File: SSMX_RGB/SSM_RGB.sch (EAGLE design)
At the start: 24 parts, among them IC1 CBT3244ADW, IC2 CBT3244ADW, IC3 CBT3244ADW, IC4 CBT3244ADW, U1 L7805C-V

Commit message: Revision
*Tied S_PWR Pos 1 to nothing (no power on this pos)
*Addressed errors and warnings in ERC
*Ran Autorouter again to fix netlist
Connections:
- net BUS_V-: no longer S_PWR.O
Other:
- moved on the sheet: R2
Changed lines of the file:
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@@
 <instance part="IC4" gate="G$1" x="8.89" y="-19.558" rot="R90"/>
 <instance part="R1" gate="G$1" x="55.88" y="101.6" rot="R90"/>
-<instance part="R2" gate="G$1" x="-12.7" y="-10.16" rot="R90"/>
+<instance part="R2" gate="G$1" x="-10.16" y="-10.16" rot="R90"/>
 <instance part="R3" gate="G$1" x="-78.74" y="76.2" rot="R270"/>
 <instance part="R4" gate="G$1" x="-27.432" y="84.328" rot="R180"/>
@@
 <net name="BUS_V-" class="0">
 <segment>
-<pinref part="S_PWR" gate="1" pin="O"/>
-<wire x1="-40.64" y1="106.68" x2="-38.1" y2="106.68" width="0.1524" layer="91"/>
-<wire x1="-38.1" y1="106.68" x2="-38.1" y2="99.06" width="0.1524" layer="91"/>
 <wire x1="-38.1" y1="99.06" x2="-55.88" y2="99.06" width="0.1524" layer="91"/>
 <wire x1="-17.78" y1="96.52" x2="-38.1" y2="96.52" width="0.1524" layer="91"/>
 <wire x1="-38.1" y1="96.52" x2="-38.1" y2="99.06" width="0.1524" layer="91"/>
-<junction x="-38.1" y="99.06"/>
 <pinref part="IC3" gate="G$1" pin="GND"/>
 <wire x1="17.78" y1="86.868" x2="15.24" y2="86.868" width="0.1524" layer="91"/>
@@
 <pinref part="IC3" gate="G$1" pin="VCC"/>
 <wire x1="17.78" y1="91.948" x2="-2.54" y2="91.948" width="0.1524" layer="91"/>
-<pinref part="IC1" gate="G$1" pin="VCC"/>
-<wire x1="-32.512" y1="40.64" x2="-32.512" y2="20.32" width="0.1524" layer="91"/>
-<wire x1="-32.512" y1="20.32" x2="-2.54" y2="20.32" width="0.1524" layer="91"/>
 <wire x1="-2.54" y1="20.32" x2="-2.54" y2="84.328" width="0.1524" layer="91"/>
-<pinref part="IC2" gate="G$1" pin="VCC"/>
 <wire x1="-2.54" y1="84.328" x2="-2.54" y2="91.948" width="0.1524" layer="91"/>
-<wire x1="-78.486" y1="20.32" x2="-78.486" y2="15.24" width="0.1524" layer="91"/>
-<wire x1="-78.486" y1="15.24" x2="-32.512" y2="15.24" width="0.1524" layer="91"/>
-<wire x1="-32.512" y1="15.24" x2="-32.512" y2="20.32" width="0.1524" layer="91"/>
-<junction x="-32.512" y="20.32"/>
-<wire x1="-32.512" y1="15.24" x2="-27.94" y2="15.24" width="0.1524" layer="91"/>
-<pinref part="IC4" gate="G$1" pin="VCC"/>
-<wire x1="25.4" y1="-22.098" x2="30.48" y2="-22.098" width="0.1524" layer="91"/>
-<wire x1="30.48" y1="-22.098" x2="30.48" y2="-2.54" width="0.1524" layer="91"/>
-<wire x1="30.48" y1="-2.54" x2="-12.7" y2="-2.54" width="0.1524" layer="91"/>
-<wire x1="-12.7" y1="-2.54" x2="-27.94" y2="-2.54" width="0.1524" layer="91"/>
-<wire x1="-27.94" y1="15.24" x2="-27.94" y2="-2.54" width="0.1524" layer="91"/>
 <pinref part="R4" gate="G$1" pin="1"/>
 <wire x1="-22.352" y1="84.328" x2="-2.54" y2="84.328" width="0.1524" layer="91"/>
 <junction x="-2.54" y="84.328"/>
-<pinref part="R2" gate="G$1" pin="2"/>
-<wire x1="-12.7" y1="-5.08" x2="-12.7" y2="-2.54" width="0.1524" layer="91"/>
-<junction x="-12.7" y="-2.54"/>
 <pinref part="R1" gate="G$1" pin="2"/>
 <wire x1="55.88" y1="116.84" x2="55.88" y2="106.68" width="0.1524" layer="91"/>
@@
 <junction x="-2.54" y="91.948"/>
 <label x="2.54" y="116.84" size="1.778" layer="95"/>
+<pinref part="IC1" gate="G$1" pin="VCC"/>
+<wire x1="-32.512" y1="40.64" x2="-38.1" y2="40.64" width="0.1524" layer="91"/>
+<wire x1="-38.1" y1="40.64" x2="-38.1" y2="20.32" width="0.1524" layer="91"/>
+<wire x1="-38.1" y1="20.32" x2="-2.54" y2="20.32" width="0.1524" layer="91"/>
+<pinref part="IC2" gate="G$1" pin="VCC"/>
+<wire x1="-78.486" y1="20.32" x2="-78.486" y2="15.24" width="0.1524" layer="91"/>
+<wire x1="-78.486" y1="15.24" x2="-38.1" y2="15.24" width="0.1524" layer="91"/>
+<wire x1="-38.1" y1="15.24" x2="-27.94" y2="15.24" width="0.1524" layer="91"/>
+<wire x1="-27.94" y1="15.24" x2="-27.94" y2="-2.54" width="0.1524" layer="91"/>
+<wire x1="-10.16" y1="-2.54" x2="-27.94" y2="-2.54" width="0.1524" layer="91"/>
+<pinref part="R2" gate="G$1" pin="2"/>
+<wire x1="-10.16" y1="-5.08" x2="-10.16" y2="-2.54" width="0.1524" layer="91"/>
+<junction x="-10.16" y="-2.54"/>
+<wire x1="30.48" y1="-2.54" x2="-10.16" y2="-2.54" width="0.1524" layer="91"/>
+<wire x1="30.48" y1="-22.098" x2="30.48" y2="-2.54" width="0.1524" layer="91"/>
+<pinref part="IC4" gate="G$1" pin="VCC"/>
+<wire x1="25.4" y1="-22.098" x2="30.48" y2="-22.098" width="0.1524" layer="91"/>
+<wire x1="-38.1" y1="20.32" x2="-38.1" y2="15.24" width="0.1524" layer="91"/>
+<junction x="-38.1" y="20.32"/>
+<junction x="-38.1" y="15.24"/>
 </segment>
 </net>
@@
 <pinref part="U1" gate="G$1" pin="IN"/>
 <wire x1="-35.56" y1="101.6" x2="-35.56" y2="106.68" width="0.1524" layer="91"/>
-</segment>
-</net>
-<net name="N$1" class="0">
-<segment>
-<pinref part="S_AV" gate="G$1" pin="3"/>
-<wire x1="12.7" y1="101.6" x2="53.34" y2="101.6" width="0.1524" layer="91"/>
-<wire x1="53.34" y1="101.6" x2="53.34" y2="83.82" width="0.1524" layer="91"/>
-<wire x1="53.34" y1="83.82" x2="55.88" y2="83.82" width="0.1524" layer="91"/>
-<pinref part="IC3" gate="G$1" pin="!EB"/>
-<pinref part="IC3" gate="G$1" pin="!EA"/>
-<wire x1="50.8" y1="91.948" x2="55.88" y2="91.948" width="0.1524" layer="91"/>
-<pinref part="R1" gate="G$1" pin="1"/>
-<wire x1="55.88" y1="96.52" x2="55.88" y2="91.948" width="0.1524" layer="91"/>
-<wire x1="55.88" y1="91.948" x2="55.88" y2="86.868" width="0.1524" layer="91"/>
-<wire x1="55.88" y1="86.868" x2="50.8" y2="86.868" width="0.1524" layer="91"/>
-<wire x1="55.88" y1="83.82" x2="55.88" y2="86.868" width="0.1524" layer="91"/>
-<junction x="55.88" y="86.868"/>
-<wire x1="12.7" y1="101.6" x2="12.7" y2="76.2" width="0.1524" layer="91"/>
-<wire x1="12.7" y1="76.2" x2="-15.24" y2="76.2" width="0.1524" layer="91"/>
-<junction x="12.7" y="101.6"/>
-<wire x1="-15.24" y1="76.2" x2="-15.24" y2="-25.4" width="0.1524" layer="91"/>
-<wire x1="-15.24" y1="-25.4" x2="-12.7" y2="-25.4" width="0.1524" layer="91"/>
-<pinref part="IC4" gate="G$1" pin="!EA"/>
-<wire x1="-12.7" y1="-22.098" x2="-7.62" y2="-22.098" width="0.1524" layer="91"/>
-<wire x1="-12.7" y1="-17.018" x2="-12.7" y2="-22.098" width="0.1524" layer="91"/>
-<pinref part="R2" gate="G$1" pin="1"/>
-<wire x1="-12.7" y1="-15.24" x2="-12.7" y2="-17.018" width="0.1524" layer="91"/>
-<pinref part="IC4" gate="G$1" pin="!EB"/>
-<wire x1="-7.62" y1="-17.018" x2="-12.7" y2="-17.018" width="0.1524" layer="91"/>
-<wire x1="-12.7" y1="-25.4" x2="-12.7" y2="-22.098" width="0.1524" layer="91"/>
-<junction x="-12.7" y="-22.098"/>
 </segment>
 </net>
@@
 </segment>
 </net>
+<net name="N$1" class="0">
+<segment>
+<pinref part="IC3" gate="G$1" pin="!EB"/>
+<pinref part="R1" gate="G$1" pin="1"/>
+<wire x1="55.88" y1="96.52" x2="55.88" y2="91.948" width="0.1524" layer="91"/>
+<pinref part="IC3" gate="G$1" pin="!EA"/>
+<wire x1="50.8" y1="91.948" x2="55.88" y2="91.948" width="0.1524" layer="91"/>
+<junction x="55.88" y="91.948"/>
+<wire x1="55.88" y1="91.948" x2="55.88" y2="86.868" width="0.1524" layer="91"/>
+<wire x1="53.34" y1="106.68" x2="53.34" y2="83.82" width="0.1524" layer="91"/>
+<wire x1="53.34" y1="83.82" x2="55.88" y2="83.82" width="0.1524" layer="91"/>
+<wire x1="55.88" y1="83.82" x2="55.88" y2="86.868" width="0.1524" layer="91"/>
+<junction x="55.88" y="86.868"/>
+<wire x1="55.88" y1="86.868" x2="50.8" y2="86.868" width="0.1524" layer="91"/>
+<wire x1="53.34" y1="106.68" x2="17.78" y2="106.68" width="0.1524" layer="91"/>
+<wire x1="17.78" y1="106.68" x2="17.78" y2="101.6" width="0.1524" layer="91"/>
+<pinref part="S_AV" gate="G$1" pin="3"/>
+<wire x1="12.7" y1="101.6" x2="12.7" y2="76.2" width="0.1524" layer="91"/>
+<wire x1="12.7" y1="76.2" x2="-12.7" y2="76.2" width="0.1524" layer="91"/>
+<wire x1="-12.7" y1="76.2" x2="-12.7" y2="46.99" width="0.1524" layer="91"/>
+<wire x1="-12.7" y1="46.99" x2="-13.97" y2="46.99" width="0.1524" layer="91"/>
+<pinref part="IC4" gate="G$1" pin="!EA"/>
+<wire x1="-10.16" y1="-22.098" x2="-7.62" y2="-22.098" width="0.1524" layer="91"/>
+<junction x="-10.16" y="-22.098"/>
+<wire x1="-10.16" y1="-22.098" x2="-13.97" y2="-22.098" width="0.1524" layer="91"/>
+<pinref part="R2" gate="G$1" pin="1"/>
+<wire x1="-10.16" y1="-15.24" x2="-10.16" y2="-17.018" width="0.1524" layer="91"/>
+<wire x1="-10.16" y1="-17.018" x2="-10.16" y2="-22.098" width="0.1524" layer="91"/>
+<junction x="-10.16" y="-17.018"/>
+<pinref part="IC4" gate="G$1" pin="!EB"/>
+<wire x1="-7.62" y1="-17.018" x2="-10.16" y2="-17.018" width="0.1524" layer="91"/>
+<wire x1="-13.97" y1="46.99" x2="-13.97" y2="-22.098" width="0.1524" layer="91"/>
+<wire x1="17.78" y1="101.6" x2="12.7" y2="101.6" width="0.1524" layer="91"/>
+<junction x="12.7" y="101.6"/>
+</segment>
+</net>
 </nets>
 </sheet>
 </sheets>
+<errors>
+</errors>
 </schematic>
 </drawing>

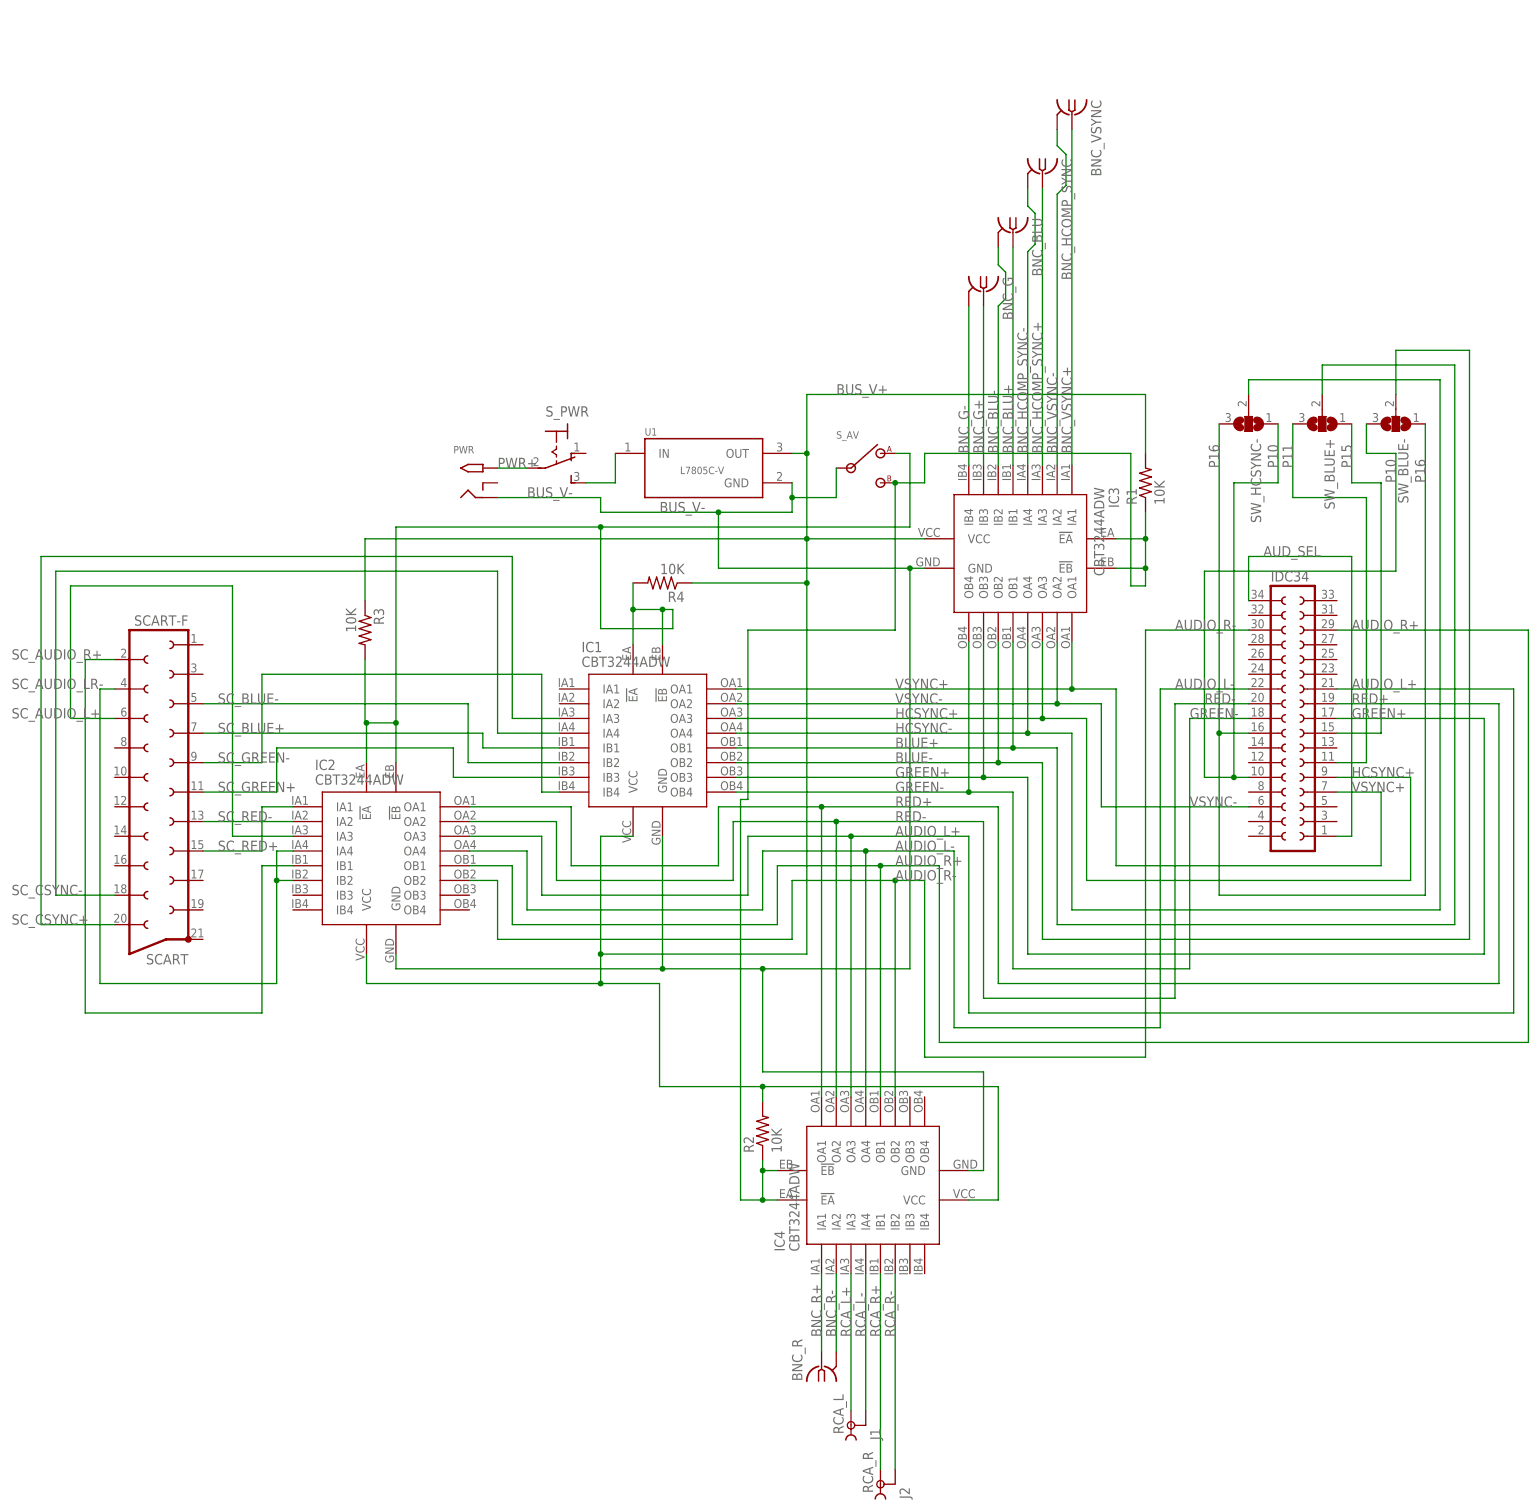
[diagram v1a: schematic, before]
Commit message: Final PCB revisions
SSM & X:
*Renamed BNC_HComp_Sync to just BNC_HCSYNC
*Renamed "Normal" cable type to "Nonstd"
*Removed stray line segs in PCB Art

SSM:
*Added warning about using both AV sources

X:
*Renamed VReg and Bus Sw IC components to Ux series
*Renamed both switchs to Sx series
*Renamed "PWR" to "J1"

Documentation:
*1st draft. Needs final product photos/images, and list of component names+parts
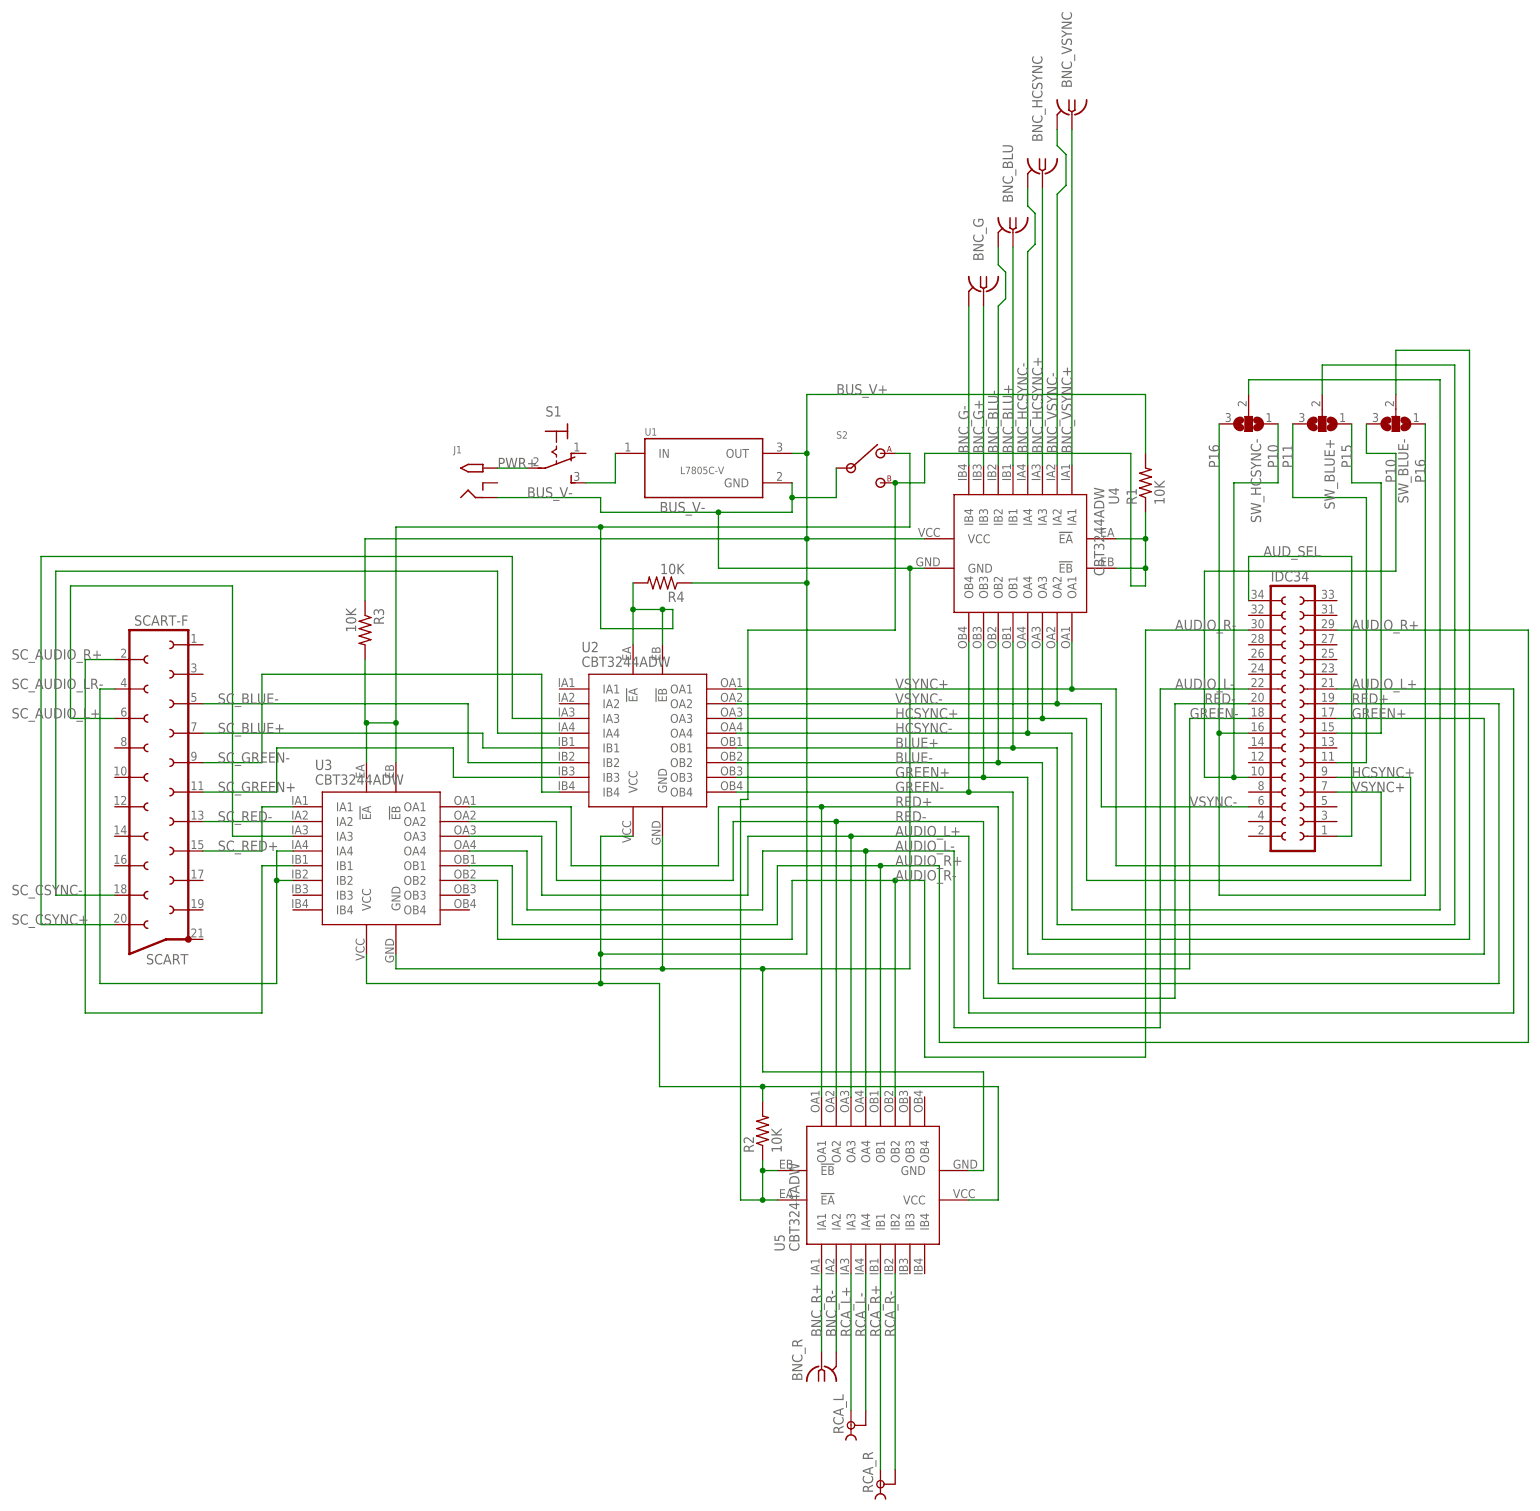
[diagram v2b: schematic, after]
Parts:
- RCA_L: value J1 -> TOBU3
- RCA_R: value J2 -> TOBU3
- renumbered BNC_HCOMP_SYNC to BNC_HCSYNC, IC1 to U2, IC2 to U3, IC3 to U4, IC4 to U5, PWR to J1, S_AV to S2, S_PWR to S1
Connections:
- net BNC_HCOMP_SYNC+ renamed BNC_HCSYNC+
- net BNC_HCOMP_SYNC- renamed BNC_HCSYNC-
